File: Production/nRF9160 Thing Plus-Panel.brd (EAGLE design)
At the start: 106.7 x 141.7 mm, 1030 parts, among them J1 USB Female C, J10 QWIIC_RIGHT_ANGLE, J11 CON-HEADER-1X16-MALE-PIN, J12 CON-1909763-1, J13 CON-1909763-1, J14 QWIIC_RIGHT_ANGLE, J15 USB Female C, J17 CON-FTSH-105-XX-X-DV, J18 CON-SIM-104224-0820, J19 CON-HEADER-1X12-MALE-PIN, J2 CON-HEADER-1X12-MALE-PIN, J20 CON-HEADER-1X16-MALE-PIN, J21 CON-1909763-1, J22 CON-1909763-1, J23 QWIIC_RIGHT_ANGLE, J24 USB Female C, J26 CON-FTSH-105-XX-X-DV, J27 CON-SIM-104224-0820, J28 CON-HEADER-1X12-MALE-PIN, J29 CON-HEADER-1X16-MALE-PIN, J3 CON-HEADER-1X16-MALE-PIN, J30 CON-1909763-1, J31 CON-1909763-1, J32 QWIIC_RIGHT_ANGLE, J33 USB Female C, J35 CON-FTSH-105-XX-X-DV, J36 CON-SIM-104224-0820, J37 CON-HEADER-1X12-MALE-PIN, J38 CON-HEADER-1X16-MALE-PIN, J39 CON-1909763-1, J4 CON-1909763-1, J40 CON-1909763-1, J41 QWIIC_RIGHT_ANGLE, J42 USB Female C, J44 CON-FTSH-105-XX-X-DV, J45 CON-SIM-104224-0820, J46 CON-HEADER-1X12-MALE-PIN, J47 CON-HEADER-1X16-MALE-PIN, J48 CON-1909763-1, J49 CON-1909763-1, J50 QWIIC_RIGHT_ANGLE, J51 USB Female C, J53 CON-FTSH-105-XX-X-DV, J54 CON-SIM-104224-0820, J55 CON-HEADER-1X12-MALE-PIN, J56 CON-HEADER-1X16-MALE-PIN, J57 CON-1909763-1, J58 CON-1909763-1, J59 QWIIC_RIGHT_ANGLE, J6 CON-SIM-104224-0820, J60 USB Female C, J62 CON-FTSH-105-XX-X-DV, J63 CON-SIM-104224-0820, J64 CON-HEADER-1X12-MALE-PIN, J65 CON-HEADER-1X16-MALE-PIN, J66 CON-1909763-1, J67 CON-1909763-1, J68 QWIIC_RIGHT_ANGLE, J69 USB Female C, J7 CON-1909763-1, J71 CON-FTSH-105-XX-X-DV, J72 CON-SIM-104224-0820, J8 CON-FTSH-105-XX-X-DV, J9 CON-HEADER-1X12-MALE-PIN, Q1 MOSFET-P-SC89, Q10 MOSFET-P-SC89, Q11 MOSFET-P-20V-4.7A-SOT23, Q12 MOSFET-DUAL-COMP-SOT563, Q13 MOSFET-N-SC89, Q14 MOSFET-N-SC89, Q15 MOSFET-P-SC89, Q16 MOSFET-P-20V-4.7A-SOT23, Q17 MOSFET-DUAL-COMP-SOT563, Q18 MOSFET-N-SC89, Q19 MOSFET-N-SC89, Q2 MOSFET-DUAL-COMP-SOT563, Q20 MOSFET-P-SC89, Q21 MOSFET-P-20V-4.7A-SOT23, Q22 MOSFET-DUAL-COMP-SOT563, Q23 MOSFET-N-SC89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

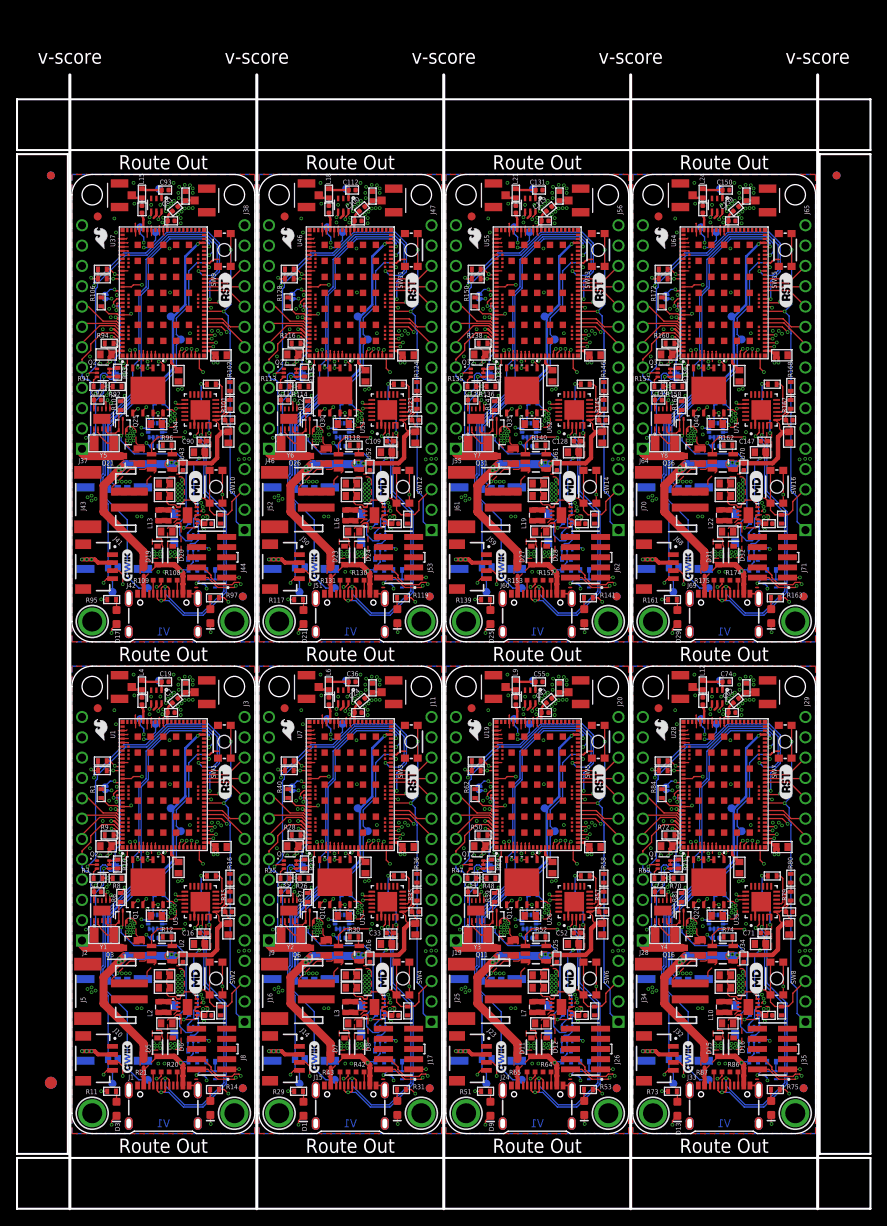
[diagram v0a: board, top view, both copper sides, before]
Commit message: Moved Panel Files
Moved panel files out of hardware folder
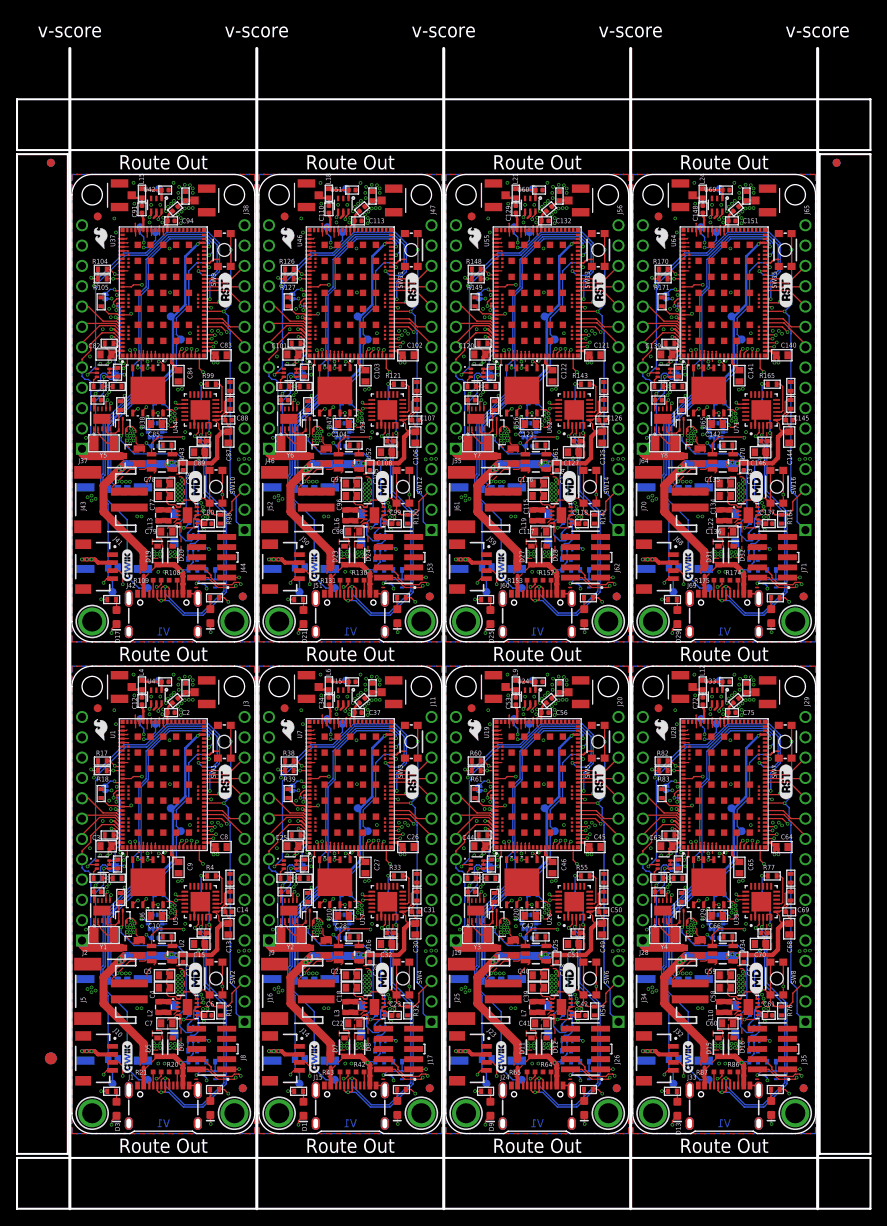
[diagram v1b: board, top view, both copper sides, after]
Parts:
- J1, J15, J24, J33, J42, J51, J60, J69: device SparkFun-Connectors:USB-C-16P-2LAYER-PADS -> SparkFun-Connectors:USB-C-16P_4LAYER-PADS
- moved E$5 3.05 mm to (-2.62, 9.40)
- moved E$6 3.05 mm to (-2.62, 9.40)
- moved E$1 1.59 mm to (-2.62, 121.3)
- moved E$2 1.59 mm to (-2.62, 121.3)
- moved E$3 1.59 mm to (95.6, 121.3)
- moved E$4 1.59 mm to (95.6, 121.3)
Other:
- board size 106.7 x 141.7 mm -> 106.7 x 145 mm
